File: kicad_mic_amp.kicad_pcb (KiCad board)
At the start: 2 copper layers, 75 x 25 mm, 35 parts, among them J1 USB_A, J2 IN_R, J3 MIC, U1 MAX9814, U2 TCR2EF36, U3 MIC5365-3.0YD5-TR, U4 PCM2906CDBR, Y1 12MHz

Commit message: Add PCB changes
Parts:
- moved R1 64.5 mm to (107.2, 58.5)
- moved R2 62.7 mm to (107.2, 63.0)
- moved R3 60.8 mm to (107.2, 67.5)
- moved C2 57.4 mm to (112.4, 54.0), turned to 180 degrees
- moved C1 57.1 mm to (107.4, 54.0)
- moved C8 49.7 mm to (128.9, 60.2), turned to 0 degrees
- moved C4 48.8 mm to (119.5, 65.9), turned to 90 degrees
- moved C3 48.3 mm to (114.8, 65.4), turned to 90 degrees
- moved C5 46.7 mm to (132.5, 69.0)
- moved U3 43.8 mm to (124.5, 60.9)
- moved C6 41.5 mm to (127.5, 54.1), turned to 90 degrees
- moved C7 36.4 mm to (121.8, 54.1), turned to 90 degrees
- moved U2 32.6 mm to (124.5, 55.5), turned to 180 degrees
- moved U1 25.4 mm to (114.0, 60.0), turned to 180 degrees
- moved J3 10.0 mm to (103.5, 54.8)
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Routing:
- net /Amplifier/*SSPND: track 0.00 -> 64.6 mm, vias 0 -> 4
- net VCC: track 9.10 -> 60.0 mm, vias 0 -> 2
- net /Amplifier/AMPOUT: track 0.00 -> 27.2 mm
- net GND: track 0.00 -> 16.0 mm, vias 0 -> 3
- net VBUS: track 52.0 -> 62.6 mm
- net Net-(U1-CG): track 0.00 -> 7.88 mm
- net /Codec/IN_R: track 30.0 -> 35.6 mm
- net Net-(U1-CT): track 0.00 -> 4.92 mm
- net /Amplifier/VBIAS: track 0.00 -> 2.62 mm

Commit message: Finish the PCB. Needs double check
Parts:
- moved R3 4.50 mm to (107.2, 63.0), turned to 180 degrees
- moved R2 3.87 mm to (110.2, 65.3), turned to 90 degrees
- turned C2 to 0 degrees
- turned JP2 to 180 degrees
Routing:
- net /Amplifier/VBIAS: track 2.62 -> 39.0 mm, vias 0 -> 2
- net VCC: track 60.0 -> 84.0 mm
- net Net-(U1-MICIN): track 0.00 -> 19.8 mm
- net Net-(JP1-B): track 0.00 -> 18.1 mm, vias 0 -> 2
- net Net-(JP2-A): track 0.00 -> 11.3 mm
- net GND: track 16.0 -> 26.5 mm, vias 3 -> 6
- net Net-(U1-BIAS): track 0.00 -> 9.45 mm
- net Net-(U1-TH): track 0.00 -> 8.76 mm
- net /Amplifier/MIC+: track 0.00 -> 8.57 mm

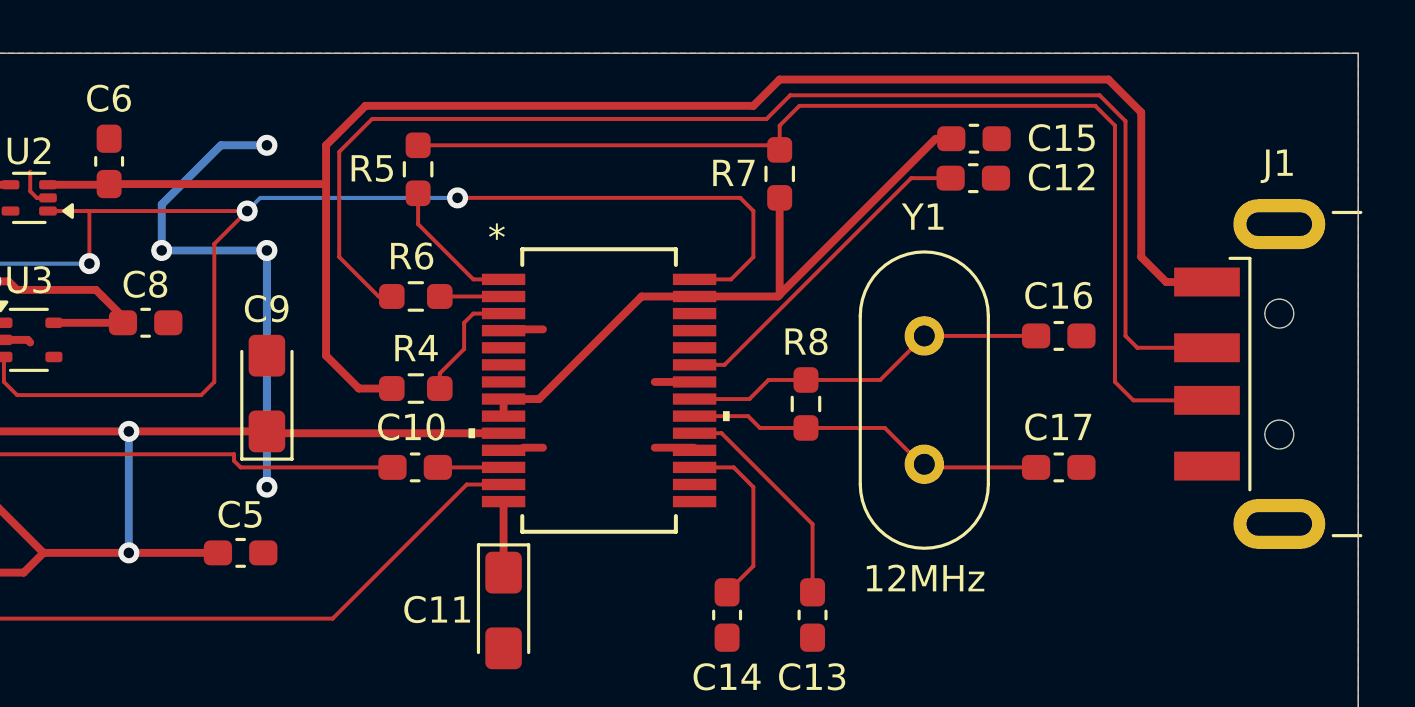
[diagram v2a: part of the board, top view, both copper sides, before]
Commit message: Correct PCB; Correct Root sheet; add PCB and 3D View pictures
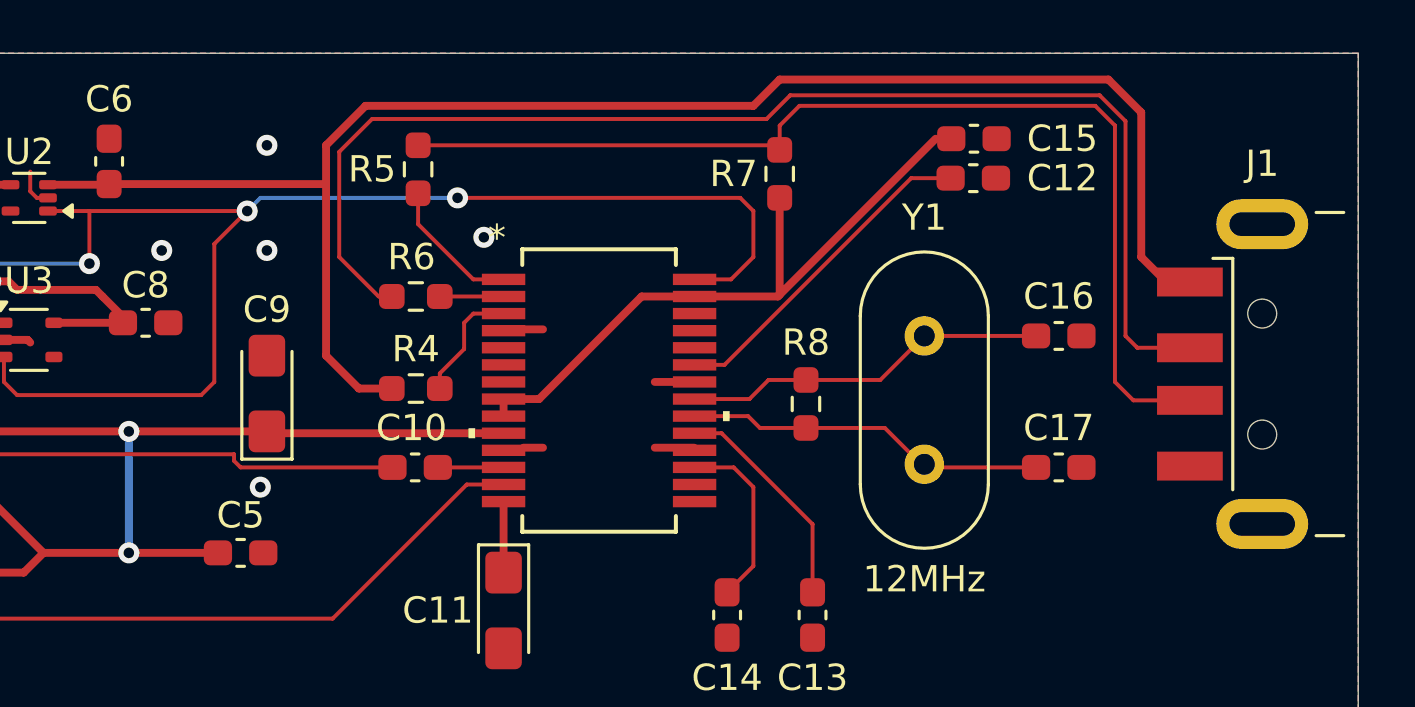
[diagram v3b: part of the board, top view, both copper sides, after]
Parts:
- moved J1 0.65 mm to (178.2, 62.2)
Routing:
- net GND: track 26.5 -> 6.85 mm, vias 6 -> 7
- net VBUS: track 62.6 -> 61.9 mm
- net /Codec/D-: track 49.3 -> 48.6 mm
- net /Codec/D+: track 41.7 -> 41.0 mm
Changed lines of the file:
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@@
 			(dashed_line_gap_ratio 3.000000)
 			(svgprecision 4)
-			(plotframeref no)
+			(plotframeref yes)
 			(mode 1)
 			(useauxorigin no)
@@
 			(dxfimperialunits yes)
 			(dxfusepcbnewfont yes)
-			(psnegative no)
+			(psnegative yes)
 			(psa4output no)
-			(plot_black_and_white yes)
+			(plot_black_and_white no)
 			(sketchpadsonfab no)
 			(plotpadnumbers no)
@@
 			(crossoutdnponfab yes)
 			(subtractmaskfromsilk no)
-			(outputformat 1)
+			(outputformat 5)
 			(mirror no)
-			(drillshape 1)
+			(drillshape 2)
 			(scaleselection 1)
 			(outputdirectory "")
@@
 	(footprint "Connector_USB:USB_A_CNCTech_1001-011-01101_Horizontal"
 		(layer "F.Cu")
-		(at 178.9 62.2)
+		(at 178.25 62.2)
 		(descr "USB type A Plug, Horizontal, http://cnctech.us/pdfs/1001-011-01101.pdf")
 		(tags "USB-A")
@@
 	)
 	(via
+		(at 141.75 57)
+		(size 0.8)
+		(drill 0.4)
+		(layers "F.Cu" "B.Cu")
+		(free yes)
+		(net 3)
+	)
+	(via
 		(at 129.5 57.5)
 		(size 0.8)
@@
 	)
 	(via
-		(at 133.5 66.5)
+		(at 133.25 66.5)
 		(size 0.8)
 		(drill 0.4)
@@
 	)
 	(segment
-		(start 133.5 66.5)
-		(end 133.5 57.5)
-		(width 0.3)
-		(layer "B.Cu")
-		(net 3)
-	)
-	(segment
 		(start 116.25 54)
 		(end 114.5 54)
@@
 	)
 	(segment
-		(start 129.5 55.75)
-		(end 131.75 53.5)
-		(width 0.3)
-		(layer "B.Cu")
-		(net 3)
-	)
-	(segment
-		(start 129.5 57.5)
-		(end 133.5 57.5)
-		(width 0.3)
-		(layer "B.Cu")
-		(net 3)
-	)
-	(segment
-		(start 131.75 53.5)
-		(end 133.5 53.5)
-		(width 0.3)
-		(layer "B.Cu")
-		(net 3)
-	)
-	(segment
-		(start 129.5 57.5)
-		(end 129.5 55.75)
-		(width 0.3)
-		(layer "B.Cu")
-		(net 3)
-	)
-	(segment
 		(start 110.574 58.324)
 		(end 110.574 59.780009)
@@
 	)
 	(segment
-		(start 169.25 58.7)
-		(end 167.7 58.7)
-		(width 0.3)
-		(layer "F.Cu")
-		(net 8)
-	)
-	(segment
 		(start 135.725 54.975)
 		(end 135.75 55)
@@
 	)
 	(segment
-		(start 125.175 55)
-		(end 127.475 55)
+		(start 167.7 58.7)
+		(end 168.6 58.7)
 		(width 0.3)
 		(layer "F.Cu")
@@
 	)
 	(segment
-		(start 135.75 53.5)
-		(end 135.75 55)
+		(start 125.175 55)
+		(end 127.475 55)
 		(width 0.3)
 		(layer "F.Cu")
@@
 	)
 	(segment
-		(start 167.7 58.7)
-		(end 166.75 57.75)
+		(start 135.75 53.5)
+		(end 135.75 55)
 		(width 0.3)
 		(layer "F.Cu")
@@
 	)
 	(segment
+		(start 166.75 57.75)
+		(end 167.7 58.7)
+		(width 0.3)
+		(layer "F.Cu")
+		(net 8)
+	)
+	(segment
 		(start 153 51)
 		(end 152 52)
@@
 	)
 	(segment
+		(start 166.45 63.2)
+		(end 168.6 63.2)
+		(width 0.15)
+		(layer "F.Cu")
+		(net 19)
+	)
+	(segment
 		(start 165.75 52.75)
 		(end 165 52)
@@
 	)
 	(segment
-		(start 169.25 63.2)
-		(end 166.45 63.2)
-		(width 0.15)
-		(layer "F.Cu")
-		(net 19)
-	)
-	(segment
 		(start 139.25 53.5)
 		(end 152.825 53.5)
@@
 	(segment
 		(start 166.601 61.2)
+		(end 168.6 61.2)
+		(width 0.15)
+		(layer "F.Cu")
+		(net 20)
+	)
+	(segment
+		(start 166.601 61.2)
 		(end 166.151 60.75)
 		(width 0.15)
@@
 		(width 0.15)
 		(layer "F.Cu")
-		(net 20)
-	)
-	(segment
-		(start 169.25 61.2)
-		(end 166.601 61.2)
-		(width 0.15)
-		(layer "F.Cu")
